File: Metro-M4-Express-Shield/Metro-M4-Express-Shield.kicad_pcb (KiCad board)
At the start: 4 copper layers, 68.9 x 53.6 mm, 20 parts, among them SW1 SW_Push, SW2 SW_Push, SW3 SW_Push, U2 ESP32-WROOM-32E

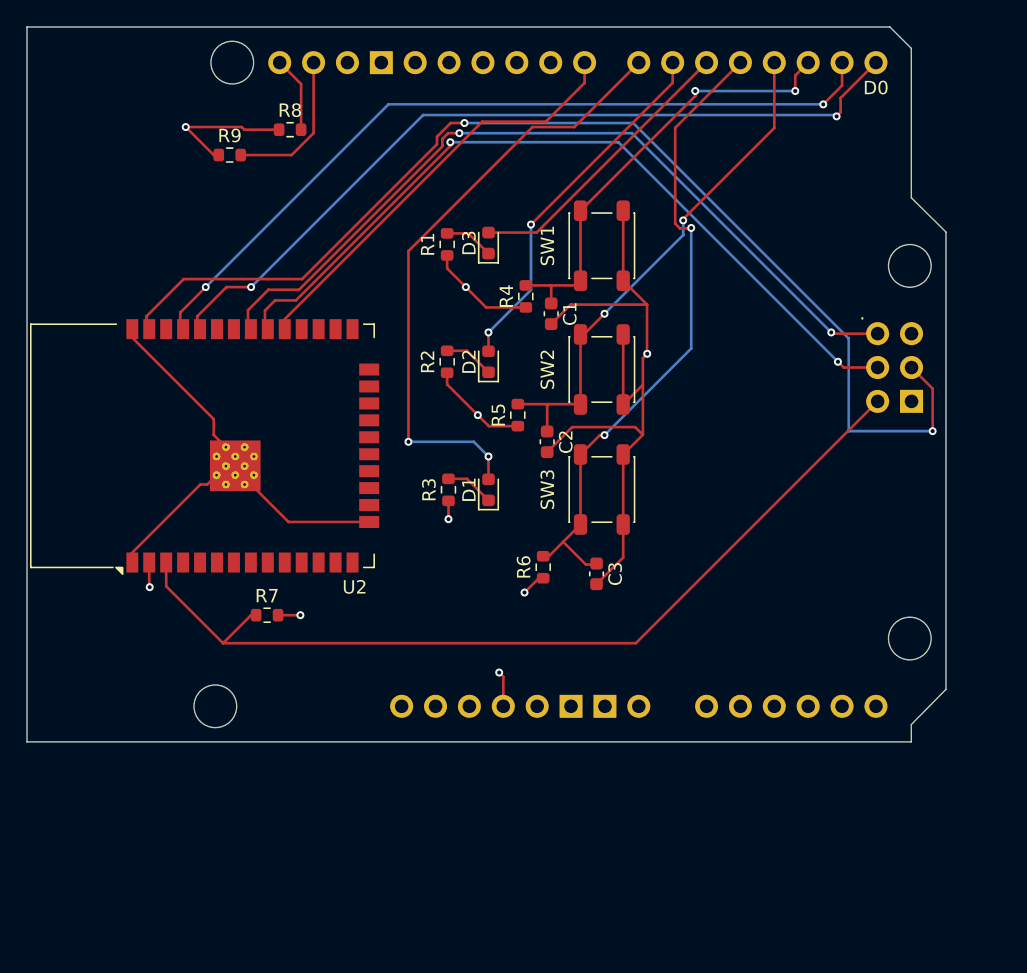
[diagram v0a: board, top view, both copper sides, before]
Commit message: add schematics, update metro shield
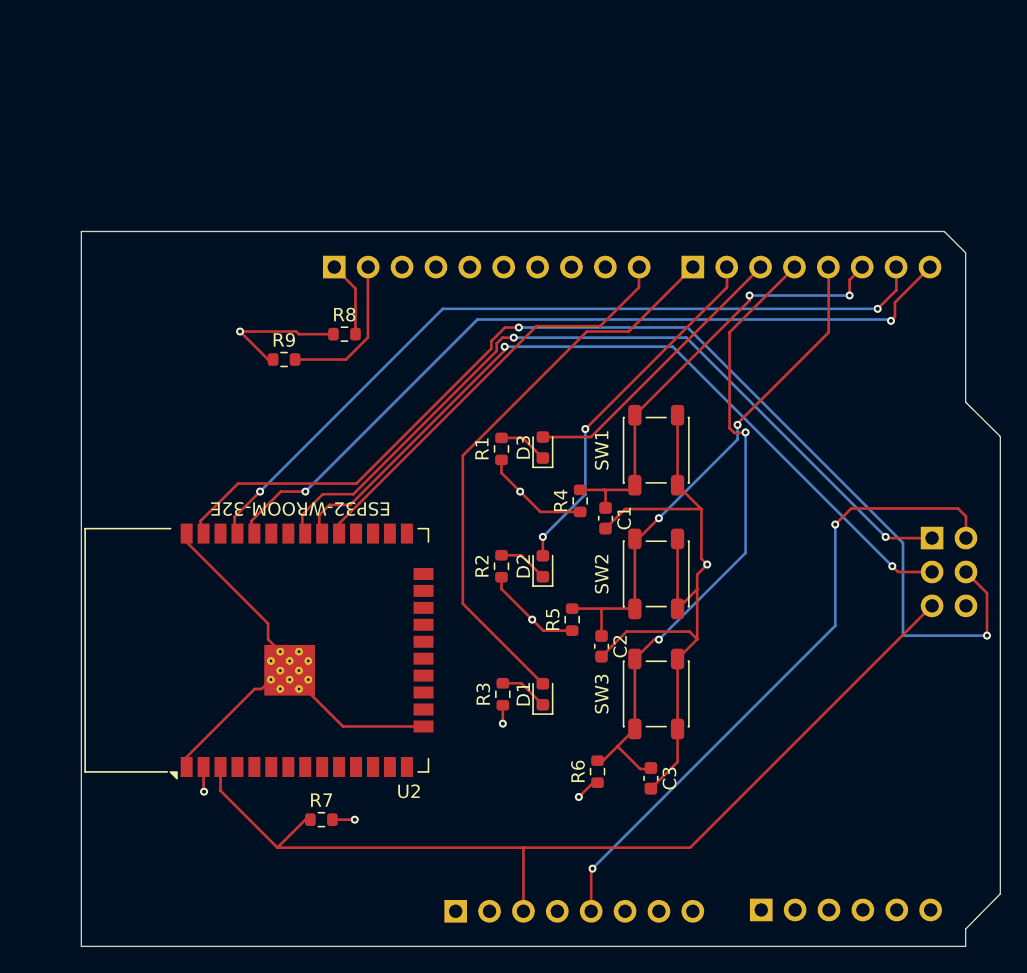
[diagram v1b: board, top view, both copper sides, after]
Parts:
- removed A1: Arduino_Uno_R3_Shield, PCM_arduino-library:Arduino_Uno_R3_Shield
- added J1: Conn_01x10, Connector_PinHeader_2.54mm:PinHeader_1x10_P2.54mm_Vertical, B.Cu at (52.3, 36.9)
- added J2: Conn_01x08, Connector_PinHeader_2.54mm:PinHeader_1x08_P2.54mm_Vertical, B.Cu at (79.2, 36.9)
- added J3: Conn_01x06, Connector_PinHeader_2.54mm:PinHeader_1x06_P2.54mm_Vertical, B.Cu at (84.3, 85.1)
- added J4: Conn_01x08, Connector_PinHeader_2.54mm:PinHeader_1x08_P2.54mm_Vertical, B.Cu at (61.4, 85.2)
- added J5: AVR-ISP-6, Connector_PinSocket_2.54mm:PinSocket_2x03_P2.54mm_Vertical, B.Cu at (97.2, 57.2)
- moved C3 15.9 mm to (76.1, 75.2)
- moved R6 15.9 mm to (72.1, 74.7)
- moved D1 15.9 mm to (68.0, 68.9)
- moved R3 15.9 mm to (65.0, 68.9)
- moved C1 15.9 mm to (72.7, 55.7)
- moved C2 15.9 mm to (72.4, 65.3)
- moved R1 15.9 mm to (64.9, 50.5)
- moved R2 15.9 mm to (64.9, 59.3)
- moved R4 15.9 mm to (70.8, 54.4)
- moved R5 15.9 mm to (70.2, 63.3)
- moved R7 15.9 mm to (51.4, 78.3)
- moved R8 15.9 mm to (53.1, 41.9)
- moved R9 15.9 mm to (48.6, 43.8)
- moved SW1 15.9 mm to (76.5, 50.6)
- moved U2 15.9 mm to (49.5, 65.6)
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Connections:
- net /SPI_RESET renamed /RESET
- U2 pad 34: /D0 -> /D0/RX
- U2 pad 35: /D1 -> /D1/TX
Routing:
- net /D0: track 60.5 -> 0.00 mm, vias 2 -> 0
- net /D0/RX: track 0.00 -> 60.5 mm, vias 0 -> 2
- net /D1/TX: track 0.00 -> 59.6 mm, vias 0 -> 2
- net /D1: track 59.6 -> 0.00 mm, vias 2 -> 0
- net /+5V_METRO: track 0.00 -> 48.7 mm, vias 0 -> 2
- net /RESET: track 67.7 -> 72.5 mm
- net +3.3V: track 35.7 -> 32.7 mm, vias 8 -> 7
- net /D7: track 45.6 -> 42.7 mm, vias 2 -> 0
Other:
- board text added: "ESP32-WROOM-32E"

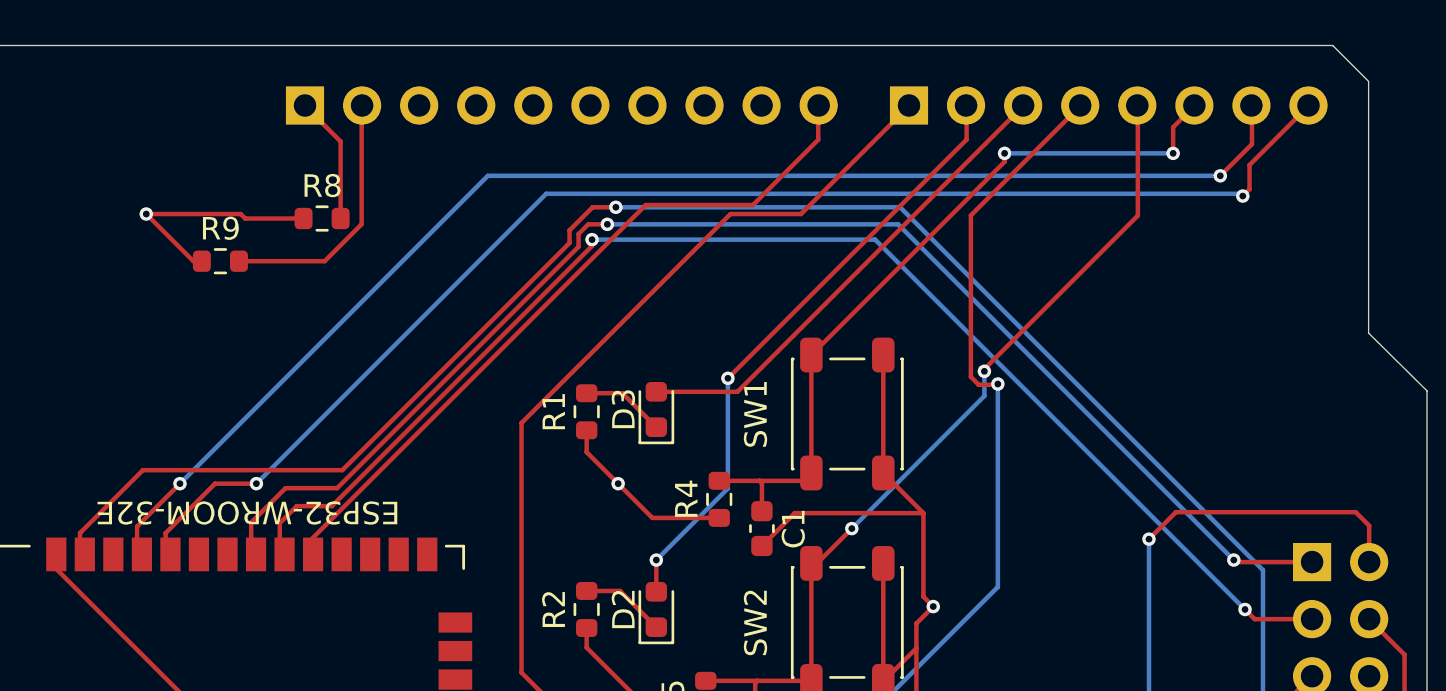
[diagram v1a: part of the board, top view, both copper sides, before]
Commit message: fix ESP32 RX/TX connection
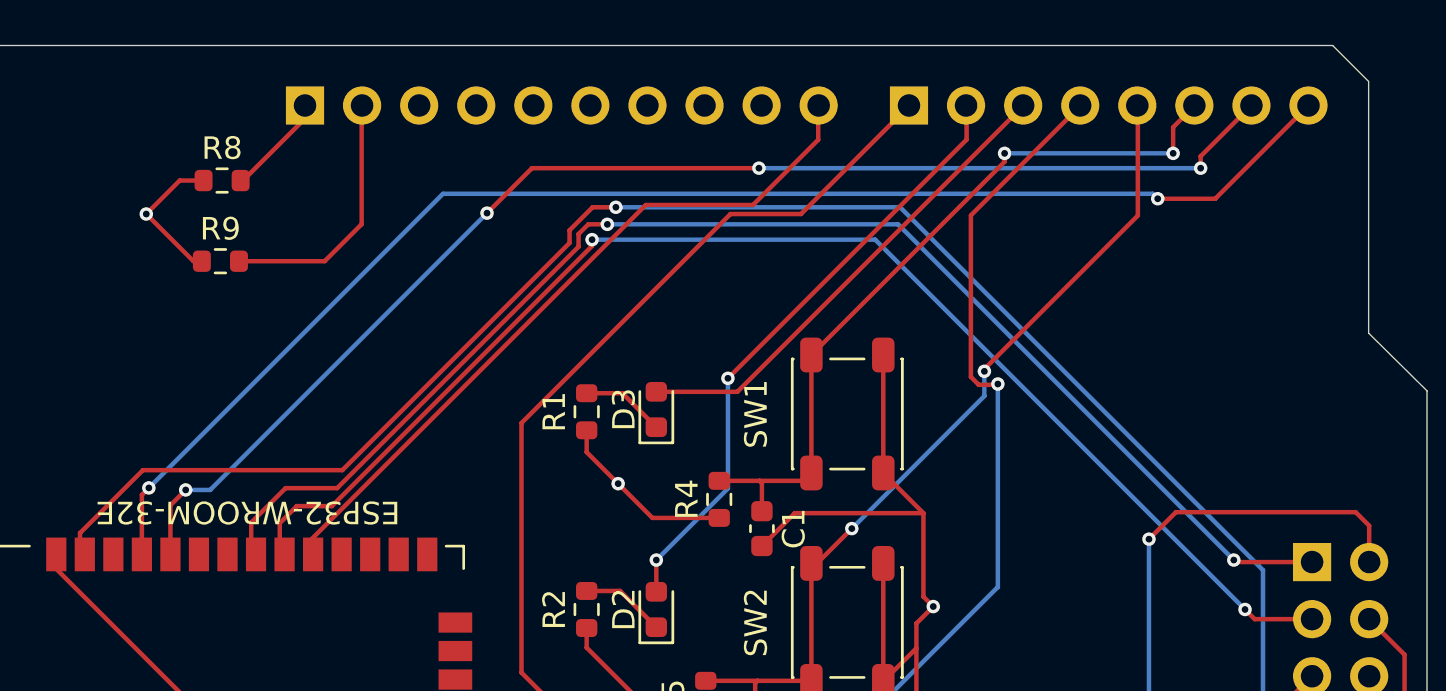
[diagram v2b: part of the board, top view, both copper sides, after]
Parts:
- moved R8 4.76 mm to (48.6, 40.2)
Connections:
- U2 pad 34: /D0/RX -> /D1/TX
- U2 pad 35: /D1/TX -> /D0/RX
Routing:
- net +3.3V: track 32.7 -> 28.8 mm
- net /D1/TX: track 59.6 -> 58.0 mm, vias 2 -> 4
- net /D0/RX: track 60.5 -> 61.9 mm
- net /SCL: track 5.69 -> 4.62 mm
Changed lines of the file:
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@@
 			(size 1.5 0.9)
 			(layers "F.Cu" "F.Mask" "F.Paste")
-			(net 61 "/D0{slash}RX")
+			(net 60 "/D1{slash}TX")
 			(pinfunction "RXD0/IO3")
 			(pintype "bidirectional")
@@
 			(size 1.5 0.9)
 			(layers "F.Cu" "F.Mask" "F.Paste")
-			(net 60 "/D1{slash}TX")
+			(net 61 "/D0{slash}RX")
 			(pinfunction "TXD0/IO1")
 			(pintype "bidirectional")
@@
 	(footprint "Resistor_SMD:R_0603_1608Metric"
 		(layer "F.Cu")
-		(at 53.100028 41.93)
+		(at 48.65 40.24)
 		(descr "Resistor SMD 0603 (1608 Metric), square (rectangular) end terminal, IPC-7351 nominal, (Body size source: IPC-SM-782 page 72, https://www.pcb-3d.com/wordpress/wp-content/uploads/ipc-sm-782a_amendment_1_and_2.pdf), generated with kicad-footprint-generator")
 		(tags "resistor")
@@
 	)
 	(segment
-		(start 53.925028 38.504119)
-		(end 52.320909 36.9)
+		(start 49.475 40.24)
+		(end 49.5 40.24)
 		(width 0.2)
 		(layer "F.Cu")
@@
 	)
 	(segment
-		(start 53.925028 41.93)
-		(end 53.925028 38.504119)
+		(start 49.5 40.24)
+		(end 49.54 40.28)
 		(width 0.2)
 		(layer "F.Cu")
@@
 	)
 	(segment
-		(start 49.675028 41.93)
-		(end 52.275028 41.93)
+		(start 52.34 37.48)
+		(end 52.34 36.9)
 		(width 0.2)
 		(layer "F.Cu")
-		(net 21)
+		(net 20)
+	)
+	(segment
+		(start 49.54 40.28)
+		(end 52.34 37.48)
+		(width 0.2)
+		(layer "F.Cu")
+		(net 20)
 	)
 	(segment
@@
 	)
 	(segment
-		(start 49.475028 41.73)
-		(end 49.675028 41.93)
+		(start 52.200028 78.33)
+		(end 53.875028 78.33)
 		(width 0.2)
 		(layer "F.Cu")
@@
 	)
 	(segment
-		(start 52.200028 78.33)
-		(end 53.875028 78.33)
+		(start 47.750028 43.83)
+		(end 47.375028 43.83)
 		(width 0.2)
 		(layer "F.Cu")
@@
 	)
 	(segment
-		(start 47.750028 43.83)
-		(end 47.375028 43.83)
+		(start 46.765028 40.24)
+		(end 45.275028 41.73)
 		(width 0.2)
 		(layer "F.Cu")
@@
 	)
 	(segment
-		(start 45.275028 41.73)
-		(end 49.475028 41.73)
+		(start 42.540028 74.38)
+		(end 42.540028 76.195)
 		(width 0.2)
 		(layer "F.Cu")
@@
 	)
 	(segment
-		(start 42.540028 74.38)
-		(end 42.540028 76.195)
+		(start 47.825 40.24)
+		(end 46.765028 40.24)
 		(width 0.2)
 		(layer "F.Cu")
@@
 	)
 	(segment
-		(start 94.484909 38.620119)
-		(end 94.484909 36.9)
+		(start 46.350028 54.689972)
+		(end 47.03 54.01)
+		(width 0.2)
+		(layer "F.Cu")
+		(net 60)
+	)
+	(segment
+		(start 60.44 41.69)
+		(end 62.44 39.69)
+		(width 0.2)
+		(layer "F.Cu")
+		(net 60)
+	)
+	(segment
+		(start 92.2 39.16)
+		(end 94.46 36.9)
 		(width 0.2)
 		(layer "F.Cu")
@@
 	)
 	(segment
-		(start 93.075028 40.03)
-		(end 94.484909 38.620119)
+		(start 62.44 39.69)
+		(end 72.54 39.69)
 		(width 0.2)
 		(layer "F.Cu")
@@
 	)
 	(segment
-		(start 44.865028 55.64)
-		(end 46.775028 53.73)
+		(start 92.2 39.69)
+		(end 92.2 39.16)
 		(width 0.2)
 		(layer "F.Cu")
@@
 	)
 	(segment
-		(start 44.865028 56.88)
-		(end 44.865028 55.64)
+		(start 46.350028 56.88)
+		(end 46.350028 54.689972)
 		(width 0.2)
 		(layer "F.Cu")
@@
 	)
 	(via
-		(at 46.775028 53.73)
+		(at 47.03 54.01)
 		(size 0.6)
 		(drill 0.3)
@@
 	)
 	(via
-		(at 93.075028 40.03)
+		(at 60.44 41.69)
 		(size 0.6)
 		(drill 0.3)
@@
 		(net 60)
 	)
-	(segment
-		(start 60.475028 40.03)
-		(end 93.075028 40.03)
-		(width 0.2)
-		(layer "B.Cu")
+	(via
+		(at 72.54 39.69)
+		(size 0.6)
+		(drill 0.3)
+		(layers "F.Cu" "B.Cu")
+		(net 60)
+	)
+	(via
+		(at 92.2 39.69)
+		(size 0.6)
+		(drill 0.3)
+		(layers "F.Cu" "B.Cu")
 		(net 60)
 	)
 	(segment
-		(start 46.775028 53.73)
-		(end 60.475028 40.03)
+		(start 48.12 54.01)
+		(end 60.44 41.69)
 		(width 0.2)
 		(layer "B.Cu")
@@
 	)
 	(segment
-		(start 48.335028 53.73)
-		(end 50.175028 53.73)
+		(start 47.03 54.01)
+		(end 48.12 54.01)
 		(width 0.2)
-		(layer "F.Cu")
-		(net 61)
+		(layer "B.Cu")
+		(net 60)
 	)
 	(segment
-		(start 46.135028 55.93)
-		(end 48.335028 53.73)
+		(start 72.54 39.69)
+		(end 92.2 39.69)
 		(width 0.2)
-		(layer "F.Cu")
-		(net 61)
+		(layer "B.Cu")
+		(net 60)
 	)
 	(segment
-		(start 94.375028 40.63)
-		(end 94.375028 39.549881)
+		(start 45.39 53.92)
+		(end 45.080028 54.229972)
 		(width 0.2)
 		(layer "F.Cu")
@@
 	)
 	(segment
-		(start 46.135028 56.88)
-		(end 46.135028 55.93)
+		(start 45.080028 54.229972)
+		(end 45.080028 56.88)
 		(width 0.2)
 		(layer "F.Cu")
@@
 	)
 	(segment
-		(start 94.375028 39.549881)
-		(end 97.024909 36.9)
+		(start 97 36.9)
+		(end 92.85 41.05)
 		(width 0.2)
 		(layer "F.Cu")
@@
 	)
 	(segment
-		(start 94.075028 40.93)
-		(end 94.375028 40.63)
+		(start 92.85 41.05)
+		(end 90.29 41.05)
 		(width 0.2)
 		(layer "F.Cu")
@@
 	)
 	(via
-		(at 50.175028 53.73)
+		(at 45.39 53.92)
 		(size 0.6)
 		(drill 0.3)
@@
 	)
 	(via
-		(at 94.075028 40.93)
+		(at 90.29 41.05)
 		(size 0.6)
 		(drill 0.3)
@@
 	)
 	(segment
-		(start 94.076028 40.929)
-		(end 94.075028 40.93)
-		(width 0.2)
-		(layer "B.Cu")
-		(net 61)
-	)
-	(segment
-		(start 50.175028 53.73)
-		(end 63.076028 40.829)
+		(start 90.069 40.829)
+		(end 58.481 40.829)
 		(width 0.2)
 		(layer "B.Cu")
@@
 	)
 	(segment
-		(start 94.076028 40.829)
-		(end 94.076028 40.929)
+		(start 58.481 40.829)
+		(end 45.39 53.92)
 		(width 0.2)
 		(layer "B.Cu")
@@
 	)
 	(segment
-		(start 63.076028 40.829)
-		(end 94.076028 40.829)
+		(start 90.29 41.05)
+		(end 90.069 40.829)
 		(width 0.2)
 		(layer "B.Cu")
